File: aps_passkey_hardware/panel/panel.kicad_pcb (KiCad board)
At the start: 2 copper layers, 68.4 x 49.3 mm, 288 parts, among them J1 USB_A, SW1 SW_Push, U1 RP2350A-QFN60, U2 TLV75512PDQNR, Y1 Crystal_GND24

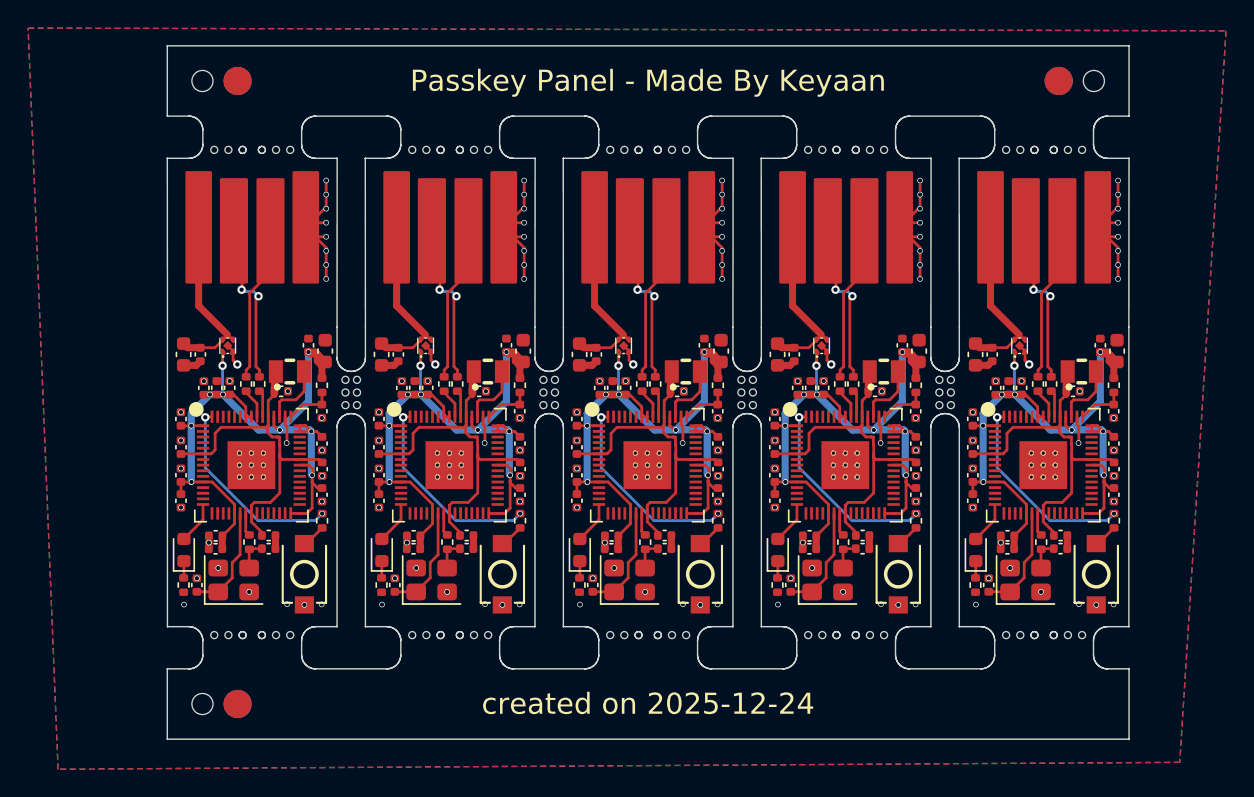
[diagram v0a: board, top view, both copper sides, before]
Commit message: fixed ground errors
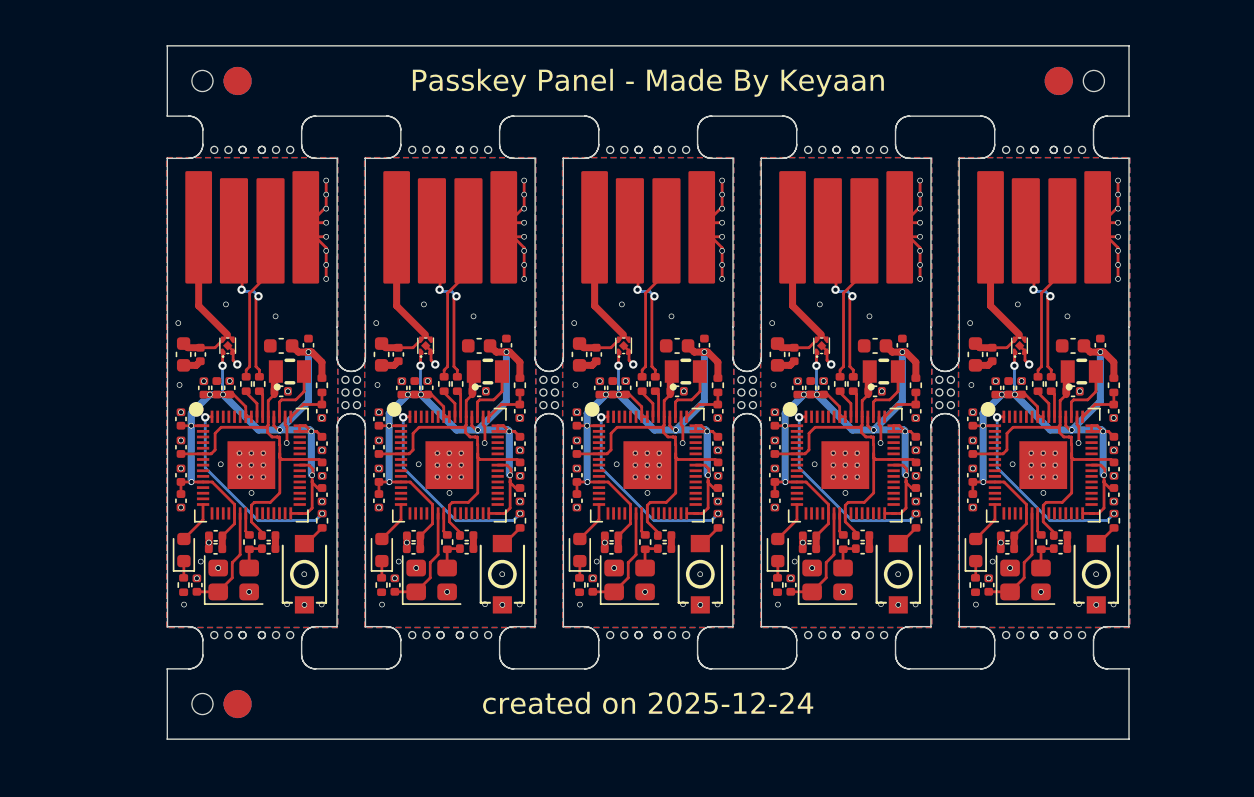
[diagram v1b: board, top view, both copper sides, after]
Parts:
- removed the C19 at (139.6, 41.7)
- removed the C19 at (153.7, 41.7)
- removed the C19 at (125.5, 41.7)
- removed the C19 at (181.8, 41.7)
- removed the C19 at (167.8, 41.7)
- added C19: 10u, Capacitor_SMD:C_0603_1608Metric, F.Cu at (178.7, 41.3)
- added C19: 10u, Capacitor_SMD:C_0603_1608Metric, F.Cu at (122.4, 41.3)
- added C19: 10u, Capacitor_SMD:C_0603_1608Metric, F.Cu at (164.6, 41.3)
- added C19: 10u, Capacitor_SMD:C_0603_1608Metric, F.Cu at (150.6, 41.3)
- added C19: 10u, Capacitor_SMD:C_0603_1608Metric, F.Cu at (136.5, 41.3)
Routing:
- net Board_1-+3V3: track 57.3 -> 56.3 mm
- net Board_2-+3V3: track 57.3 -> 56.3 mm
- net Board_4-+3V3: track 57.3 -> 56.3 mm
- net Board_3-+3V3: track 57.3 -> 56.3 mm
- net Board_0-+3V3: track 57.3 -> 56.3 mm
- net Board_3-GND: vias 29 -> 37
- net Board_0-GND: vias 29 -> 37
- net Board_4-GND: vias 29 -> 37
- net Board_2-GND: vias 29 -> 37
- net Board_1-GND: vias 29 -> 37
- added copper zone on B.Cu, net Board_1-GND
- added copper zone on F.Cu, net Board_1-GND
- added copper zone on B.Cu, net Board_2-GND
- added copper zone on F.Cu, net Board_2-GND
- added copper zone on B.Cu, net Board_3-GND
- added copper zone on F.Cu, net Board_3-GND
- added copper zone on B.Cu, net Board_4-GND
- added copper zone on F.Cu, net Board_4-GND
